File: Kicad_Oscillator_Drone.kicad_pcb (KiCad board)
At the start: 2 copper layers, 50.8 x 100.1 mm, 61 parts, among them J1 Power Out, J10 AudioJack, J11 AudioJack, J12 AudioJack, J14 AudioJack, J15 AudioJack, J17 AudioJack, J2 Power Out, J3 Jack-DC, J4 OSC1CV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

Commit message: 3D Updated
3D Models
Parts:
- added REF**: OSHW-Logo2_7.3x6mm_SilkScreen, Symbol:OSHW-Logo2_7.3x6mm_SilkScreen, F.Cu at (151.4, 111.3)
- added REF**: Gauge_100mm_Type1_SilkScreenTop, Calibration_Scale:Gauge_100mm_Type1_SilkScreenTop, B.Cu at (147.3, 22.9)
- moved D1 39.8 mm to (137.7, 101.1), turned to 180 degrees
- moved C10 33.1 mm to (137.9, 37.6)
- moved TP5 16.4 mm to (150.9, 95.5)
- moved C2 14.7 mm to (150.9, 91.4)
- moved R6 14.7 mm to (135.1, 75.9), turned to 90 degrees
- moved R4 14.2 mm to (150.9, 87.4)
- moved R7 11.4 mm to (130.3, 75.9), turned to 90 degrees
- moved C12 8.19 mm to (130.6, 88.4), turned to 0 degrees
- moved Q4 8.03 mm to (130.6, 83.8)
- moved C8 7.38 mm to (137.9, 33.0), turned to 180 degrees
- moved C13 7.18 mm to (128.5, 95.5)
- moved TP16 7.11 mm to (134.1, 96.5)
- moved D2 2.89 mm to (136.1, 107.2)
- moved R3 1.14 mm to (142.7, 108.2)
- moved R10 0.58 mm to (142.7, 104.1), turned to 270 degrees
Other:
- board text added: "Promesoft DRone One 2018-12-15 Rev A"
- board text added: "REV A Dec 2018"

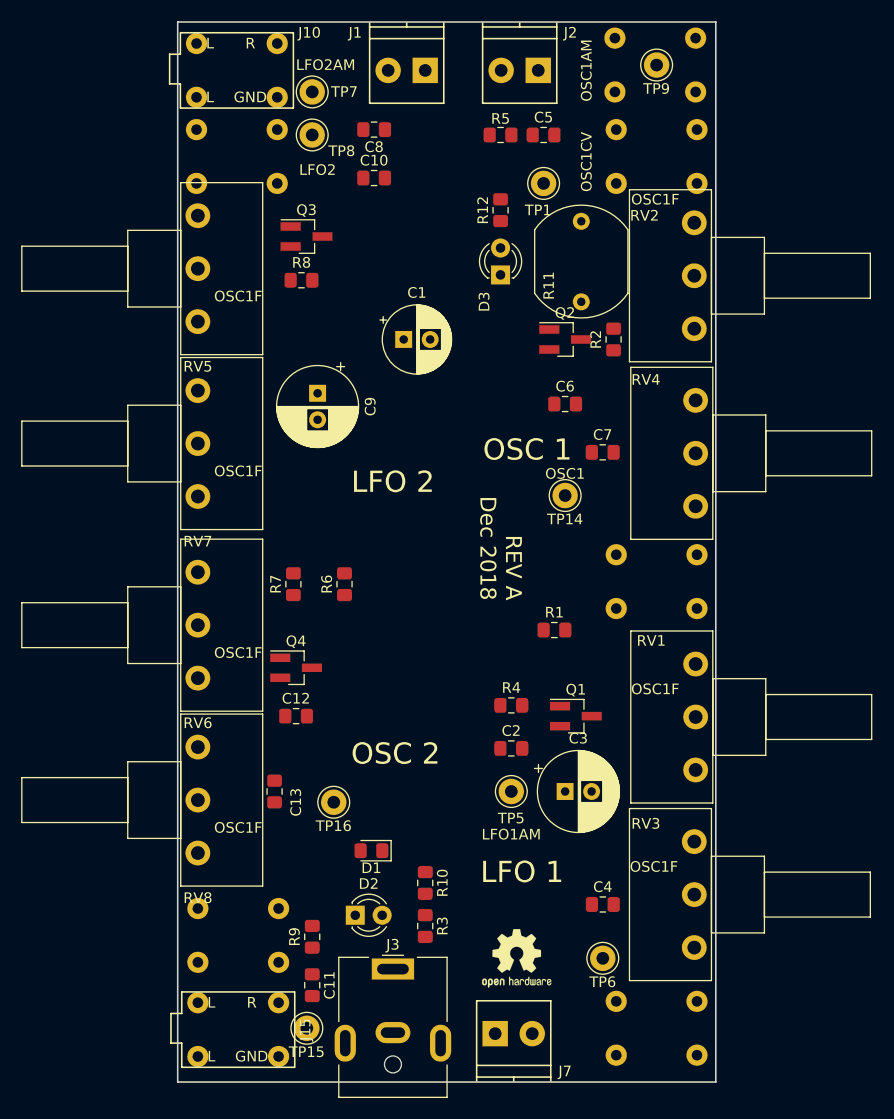
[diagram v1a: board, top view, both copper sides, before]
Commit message: Routing started LFO2 OSC1
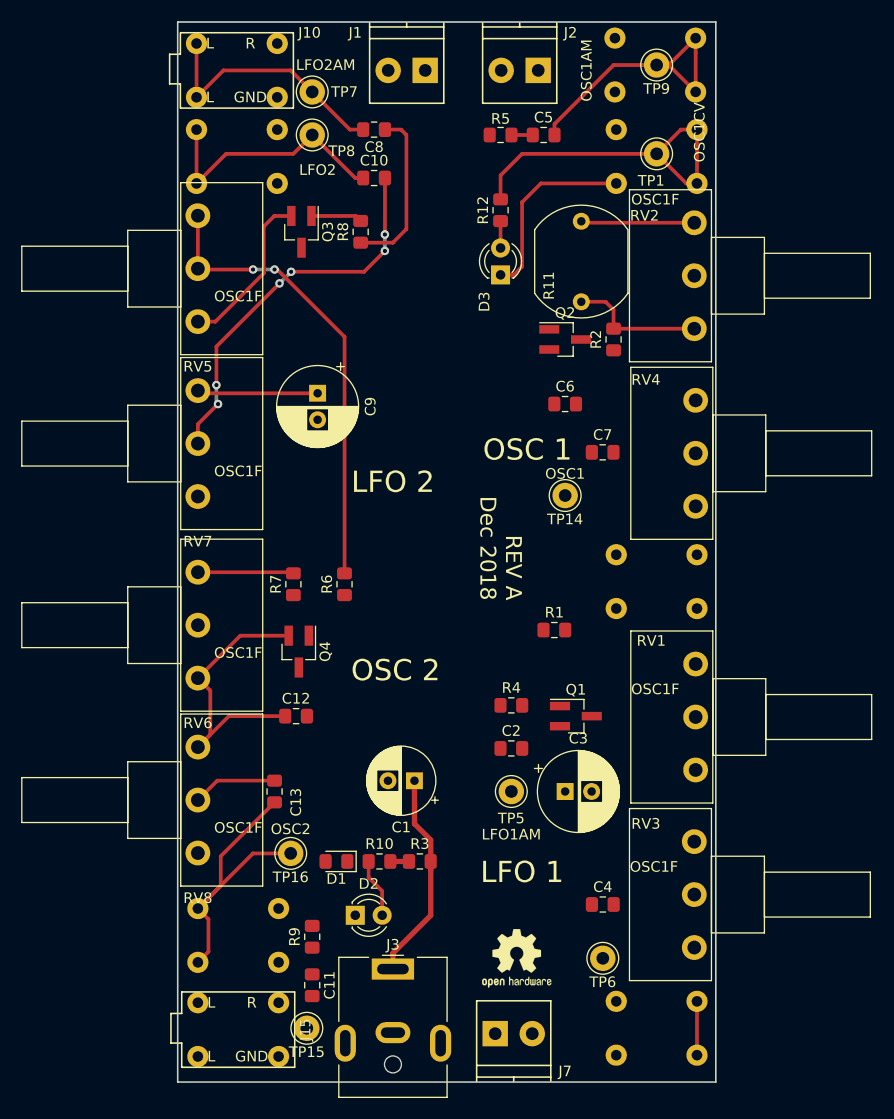
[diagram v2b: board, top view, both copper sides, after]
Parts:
- moved C1 41.7 mm to (141.7, 94.5), turned to 180 degrees
- moved TP1 11.0 mm to (164.6, 35.3)
- moved R8 7.22 mm to (136.7, 42.7), turned to 90 degrees
- moved TP16 6.31 mm to (130.0, 101.3)
- moved R3 6.12 mm to (142.2, 102.1), turned to 0 degrees
- moved R10 4.77 mm to (138.4, 102.1), turned to 0 degrees
- moved D1 3.45 mm to (134.4, 102.1)
- moved Q4 1.55 mm to (130.8, 82.3), turned to 270 degrees
- moved Q3 0.66 mm to (131.1, 42.7), turned to 270 degrees
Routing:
- net Net-(R6-Pad2): track 0.00 -> 43.8 mm, vias 0 -> 2
- net Net-(C10-Pad2): track 0.00 -> 36.5 mm, vias 0 -> 6
- net /OSC1_CV: track 0.00 -> 32.6 mm
- net OSC2-OUT: track 0.00 -> 29.9 mm
- net /OSC2: track 0.00 -> 27.2 mm
- net /LFO2: track 0.00 -> 27.0 mm
- net OSC1-AM: track 0.00 -> 26.4 mm
- net LFO2-OUT: track 0.00 -> 24.4 mm
- net LFO2-AM: track 0.00 -> 24.2 mm
- net /DC_in: track 0.00 -> 19.9 mm
- net Net-(D3-Pad1): track 0.00 -> 18.1 mm
- net Net-(C8-Pad1): track 0.00 -> 16.0 mm
- net Net-(R11-Pad1): track 0.00 -> 12.8 mm
- net /OSC1: track 0.00 -> 10.7 mm
- net Net-(R7-Pad2): track 0.00 -> 9.06 mm
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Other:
- net class Default: trace_width 0.25 -> 0.35
- net class Power added: clearance 0.2, trace_width 0.5, via_dia 0.8, via_drill 0.4

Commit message: Rev A done
Ground planes
Mounting holes
DRC
Labels
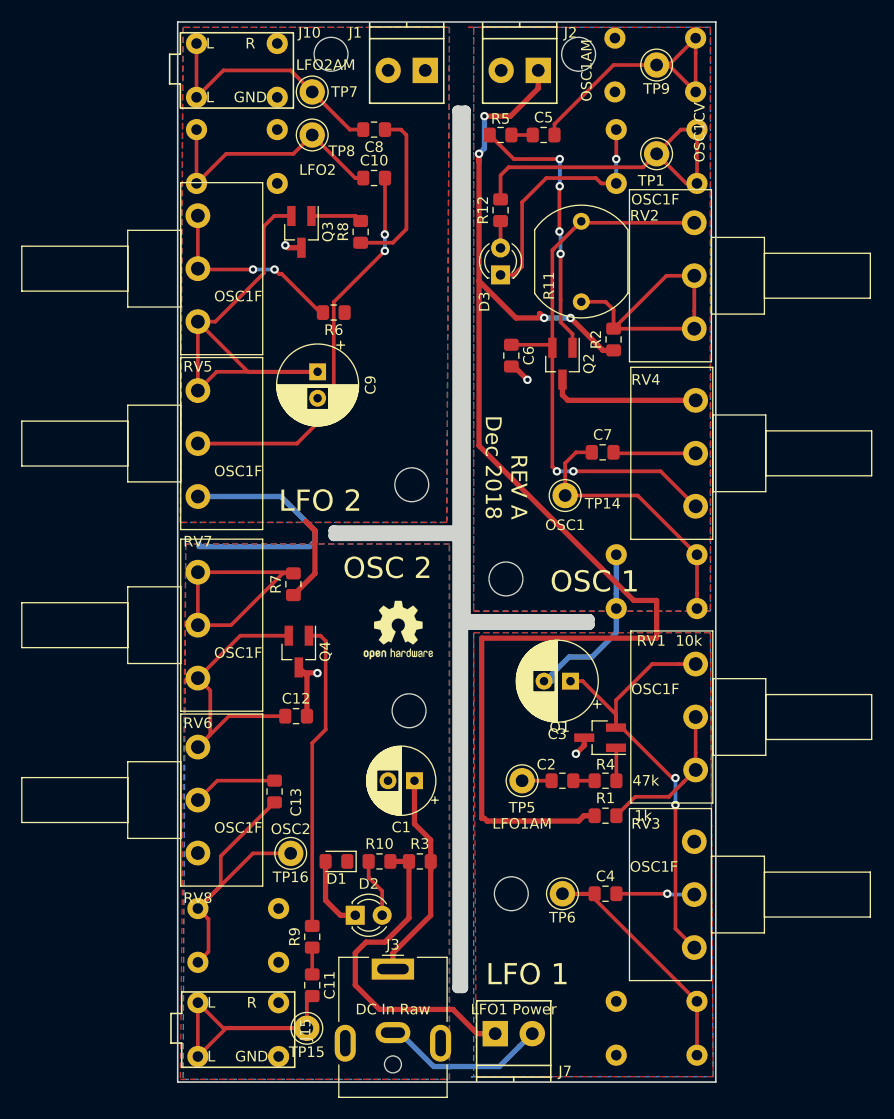
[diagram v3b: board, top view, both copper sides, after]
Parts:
- added REF**: MountingHole_3.2mm_M3, MountingHole:MountingHole_3.2mm_M3, F.Cu at (150.4, 75.4)
- added REF**: MountingHole_3.2mm_M3, MountingHole:MountingHole_3.2mm_M3, F.Cu at (133.9, 25.9)
- added REF**: MountingHole_3.2mm_M3, MountingHole:MountingHole_3.2mm_M3, F.Cu at (157.2, 25.9)
- added REF**: MountingHole_3.2mm_M3, MountingHole:MountingHole_3.2mm_M3, F.Cu at (141.5, 66.5)
- added REF**: MountingHole_3.2mm_M3, MountingHole:MountingHole_3.2mm_M3, F.Cu at (141.2, 87.9)
- added REF**: MountingHole_3.2mm_M3, MountingHole:MountingHole_3.2mm_M3, F.Cu at (150.9, 105.2)
- J3: value Jack-DC -> DC In Raw
- moved REF** 32.9 mm to (140.2, 80.3)
- moved R6 25.7 mm to (134.1, 50.3), turned to 180 degrees
- moved R1 18.2 mm to (159.8, 97.8)
- moved R4 11.4 mm to (159.8, 94.5)
- moved C3 10.4 mm to (156.5, 85.1), turned to 180 degrees
- moved TP6 7.19 mm to (155.7, 105.2)
- moved C6 6.83 mm to (150.9, 54.4), turned to 270 degrees
- moved C2 5.71 mm to (155.7, 94.5), turned to 180 degrees
- moved Q1 3.06 mm to (159.3, 90.4), turned to 180 degrees
- moved Q2 2.30 mm to (155.7, 55.1), turned to 270 degrees
- moved C9 2.03 mm to (132.6, 55.9)
- moved TP5 1.44 mm to (151.9, 94.5)
- moved C4 1.05 mm to (159.8, 105.2)
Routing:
- net +10V: track 1.76 -> 166.7 mm, vias 0 -> 4
- net GND: track 0.00 -> 90.0 mm, vias 0 -> 4
- net /OSC1: track 10.7 -> 54.1 mm, vias 0 -> 2
- net /LFO1: track 0.00 -> 41.9 mm, vias 0 -> 2
- net OSC2-AM: track 0.00 -> 31.0 mm
- net Net-(Q4-Pad1): track 0.00 -> 29.2 mm
- net Net-(Q2-Pad1): track 0.00 -> 25.9 mm, vias 0 -> 4
- net OSC1-OUT: track 0.00 -> 25.8 mm
- net Net-(R6-Pad2): track 43.8 -> 18.5 mm
- net /LFO2: track 27.0 -> 47.7 mm
- net LFO1-OUT: track 5.08 -> 25.0 mm
- net Net-(R7-Pad2): track 9.06 -> 25.1 mm
- net Net-(R11-Pad1): track 12.8 -> 27.4 mm
- net Net-(R1-Pad2): track 0.00 -> 14.3 mm
- net Net-(C7-Pad2): track 0.00 -> 7.79 mm
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- added copper zone on F.Cu, net +10V
- added copper zone on B.Cu, net GND
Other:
- outline, holes or cut-outs redrawn
